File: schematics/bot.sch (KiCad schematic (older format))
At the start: 70 parts, among them J1 LED Matrix, J2 LED Matrix, J3 USB_B, M1 Motor_Servo, M2 Motor_Servo, Q1 2N7000, Q2 2N7000, Q3 2N7000, Q4 2N7000, Q5 2N3906, Q6 2N7000, Q7 2N7000, Q8 IRF6614, U1 74HC595, U2 74HC595, U3 74HC595, U4 74HC595, U5 AMS1117-3.3, U6 CP2102N-A01-GQFN24, U7 STM32F103C8Tx, Y1 8MHz

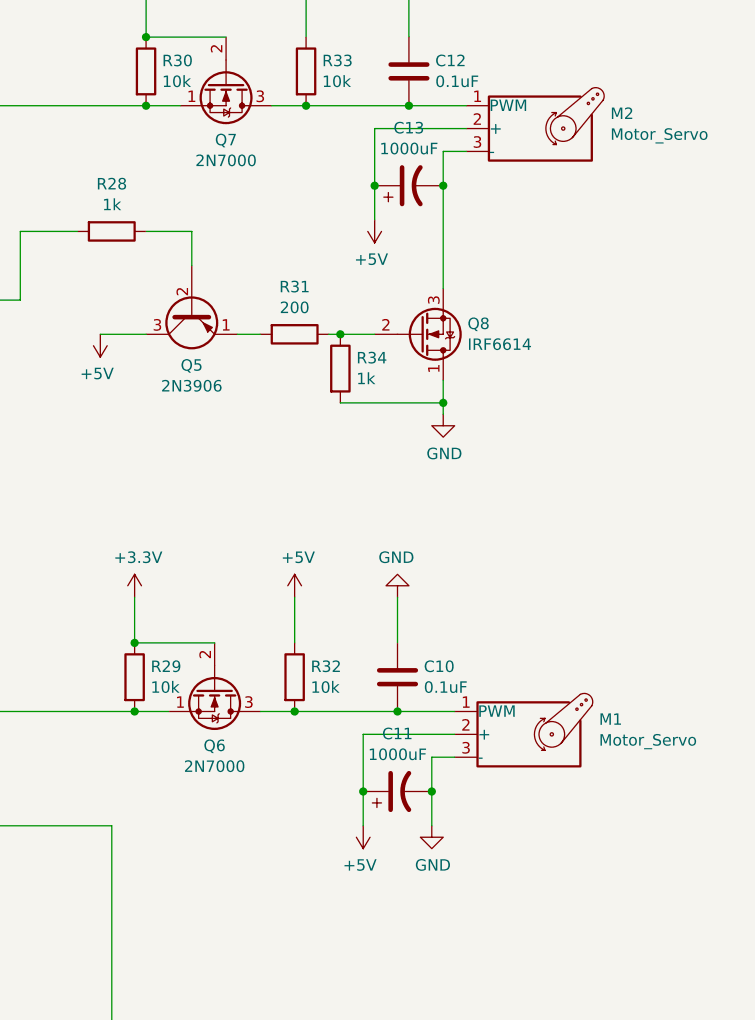
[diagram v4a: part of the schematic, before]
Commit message: Add decoupling capacitors
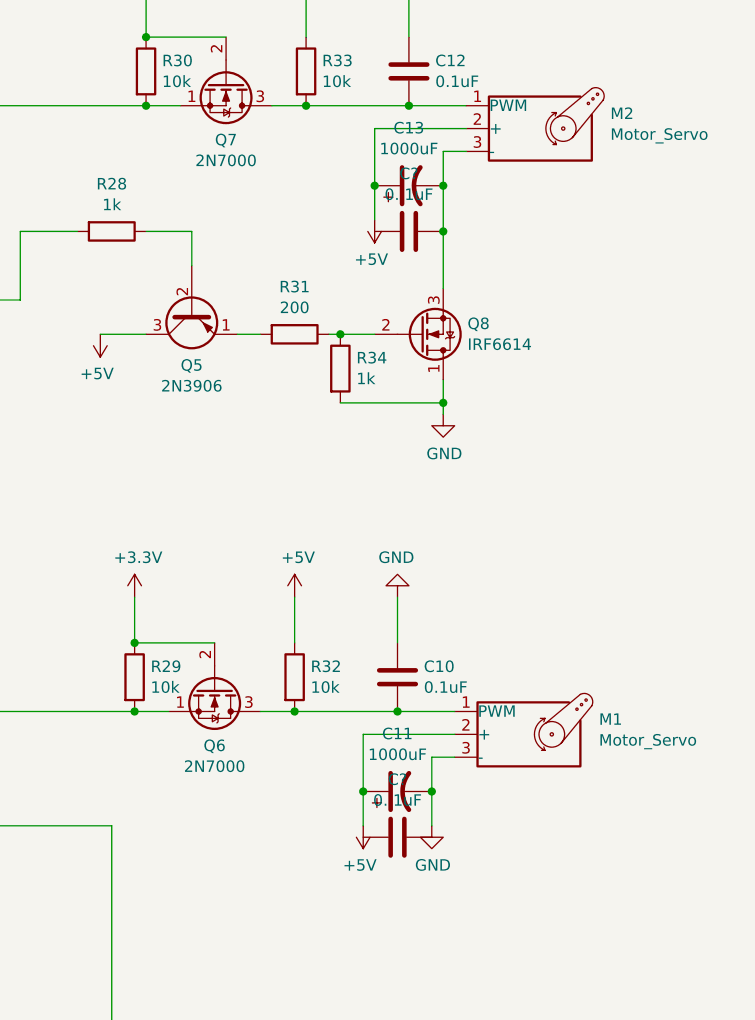
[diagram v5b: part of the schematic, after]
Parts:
- added C? (x2): 0. 1uF, symbol Device:C
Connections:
- net at C13.2, M2.3 (-), Q8.3 (S): now also C?.2
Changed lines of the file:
@@
 	14200 4550 14200 4700
 Wire Wire Line
-	14200 4700 14200 5150
+	14200 4700 14200 4900
 Connection ~ 14200 4700
 $Comp
@@
 	0    1    1    0
 $EndComp
+$Comp
+L Device:C C?
+U 1 1 5BDF5D3B
+P 14050 4900
+F 0 "C?" V 14302 4900 50  0000 C CNN
+F 1 "0. 1uF" V 14211 4900 50  0000 C CNN
+F 2 "" H 14088 4750 50  0001 C CNN
+F 3 "~" H 14050 4900 50  0001 C CNN
+	1    14050 4900
+	0    -1   -1   0
+$EndComp
+Connection ~ 14200 4900
+Wire Wire Line
+	14200 4900 14200 5150
+$Comp
+L Device:C C?
+U 1 1 5BDF602E
+P 14000 7550
+F 0 "C?" V 14252 7550 50  0000 C CNN
+F 1 "0. 1uF" V 14161 7550 50  0000 C CNN
+F 2 "" H 14038 7400 50  0001 C CNN
+F 3 "~" H 14000 7550 50  0001 C CNN
+	1    14000 7550
+	0    -1   -1   0
+$EndComp
 $EndSCHEMATC
